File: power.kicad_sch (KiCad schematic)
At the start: 65 parts, among them Q10 2NPN, Q3 PMOS, Q4 PMOS, Q5 PMOS, Q6 PMOS, Q7 2NPN, Q9 2PNP, U21 TPS62410, U22 LDO-2V5

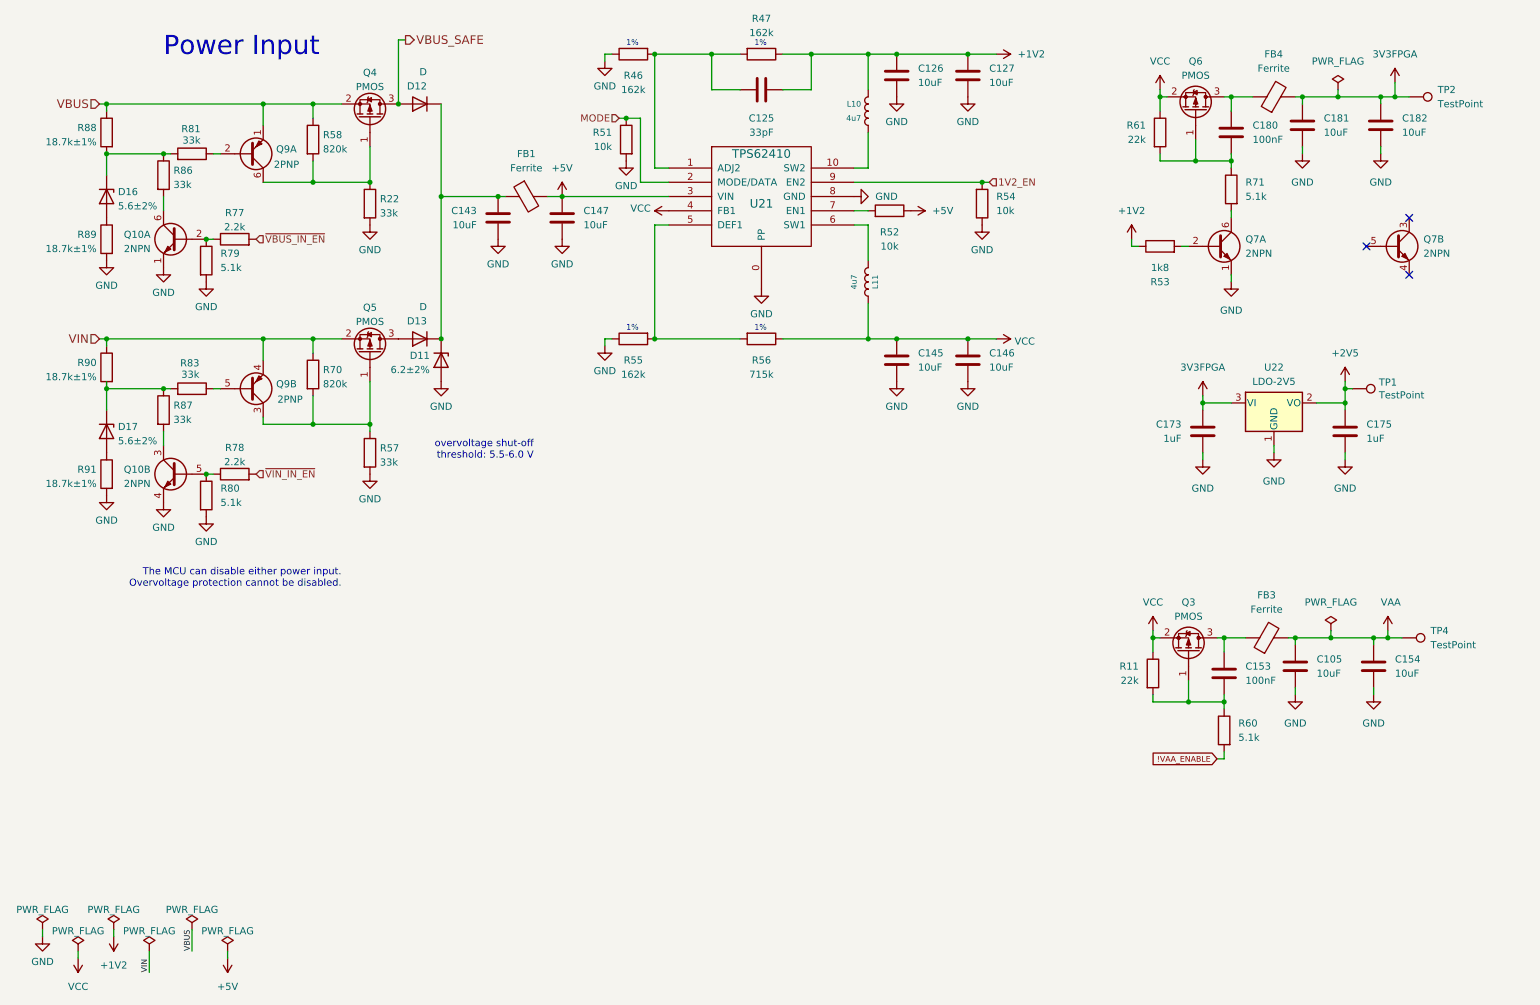
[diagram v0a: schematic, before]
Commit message: Rearrange RF section
- Use DPDT RF switches to reduce long tracks
- Add limiter
- Add switch control logic
- Move ADC/DAC U18 to RF area
- Remove baseband header P9
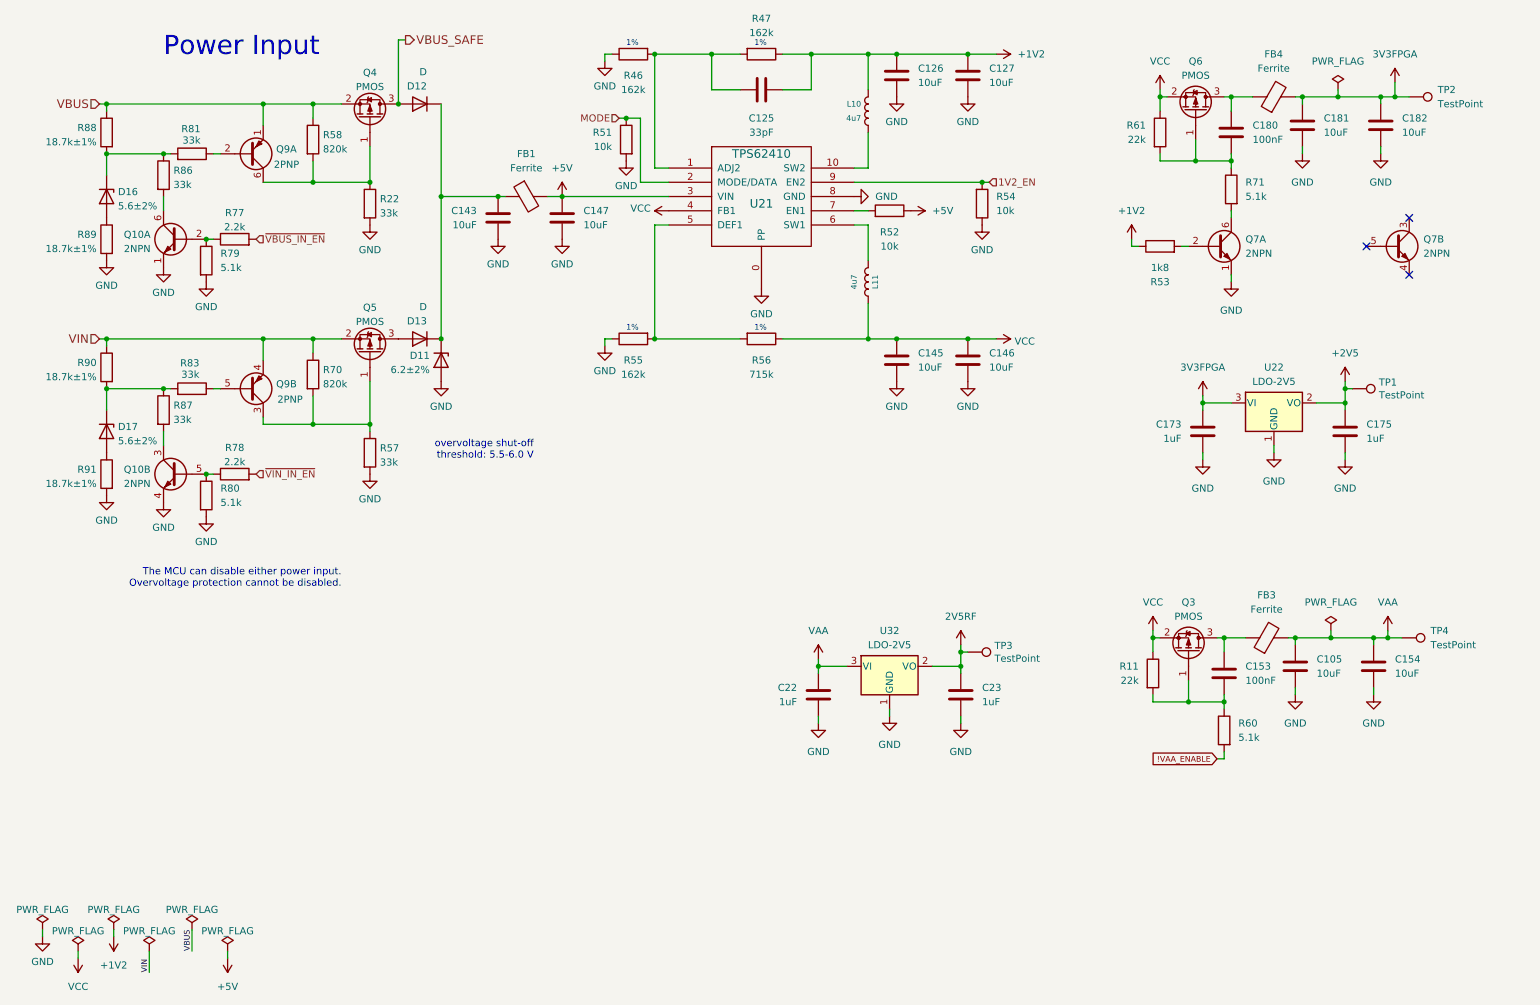
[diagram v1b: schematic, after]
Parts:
- added C22, C23: 1uF, Capacitor_SMD:C_0402_1005Metric, symbol Device:C
- added TP3: TestPoint, TestPoint:TestPoint_Pad_D1.0mm, symbol Connector:TestPoint
- added U32: LDO-2V5, Package_TO_SOT_SMD:SOT-23-3, symbol Regulator_Linear:XC6206PxxxMR
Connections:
- net GND: now also C22.2, C23.2, U32.1 (GND)
- net VAA: now also C22.1, U32.3 (VI)
- new net 2V5RF: C23.1, TP3.1, U32.2 (VO)

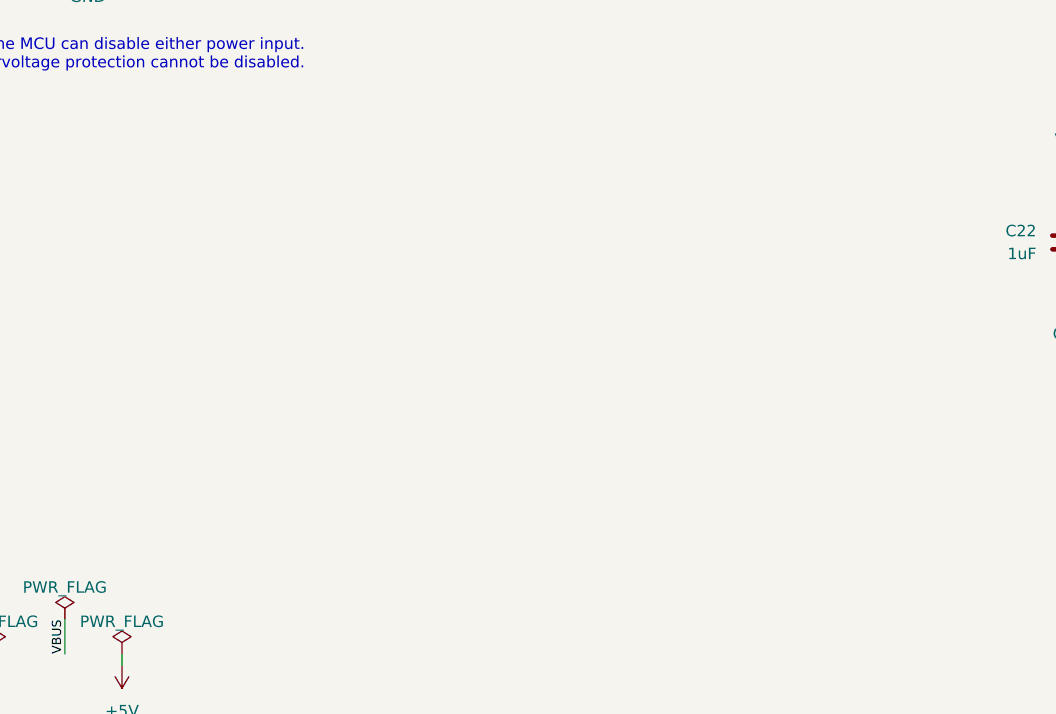
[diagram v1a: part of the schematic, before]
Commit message: Add current-limiting switch to expansion interface
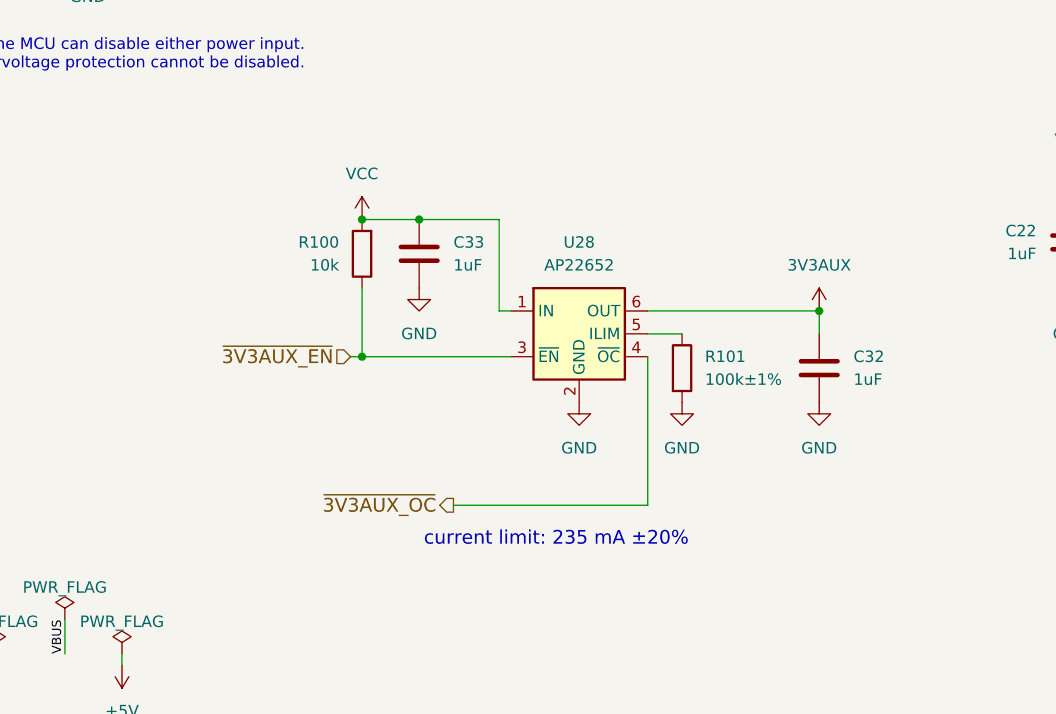
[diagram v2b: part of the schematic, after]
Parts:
- added C32, C33: 1uF, Capacitor_SMD:C_0402_1005Metric, symbol Device:C
- added R100: 10k, Resistor_SMD:R_0402_1005Metric, symbol Device:R
- added R101: 100k±1%, Resistor_SMD:R_0402_1005Metric, symbol Device:R
- added U28: AP22652, Package_SO:TSOP-6_1.65x3.05mm_P0.95mm, symbol Power_Management:BD2243G
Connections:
- net GND: now also C32.2, C33.2, R101.2, U28.2 (GND)
- net VCC: now also C33.1, R100.2, U28.1 (IN)
- new net: R101.1, U28.5 (ILIM)
- new net 3V3AUX: C32.1, U28.6 (OUT)
- new net ~{3V3AUX_EN}: R100.1, U28.3 (~{EN})
- new net ~{3V3AUX_OC}: U28.4 (~{OC})
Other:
- note added: "current limit: 235 mA ±20%"

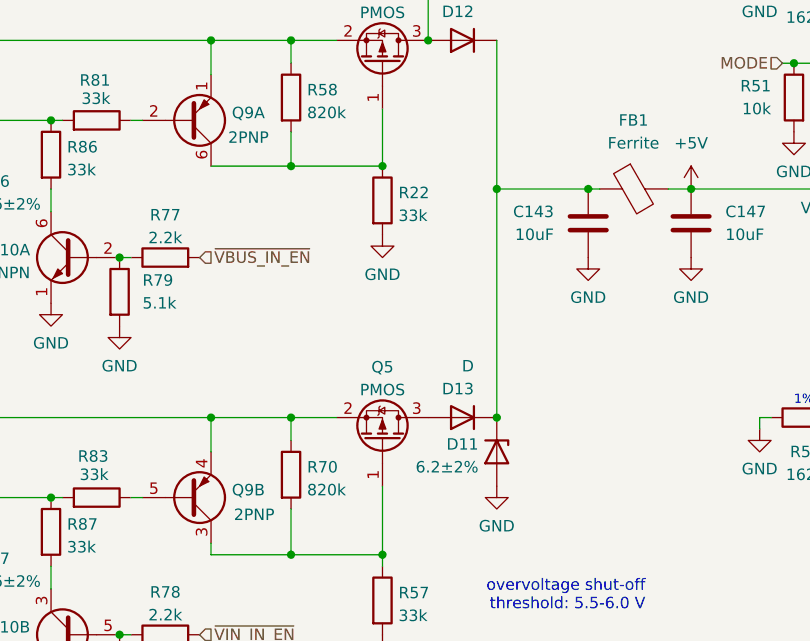
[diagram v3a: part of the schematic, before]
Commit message: Change Type-C controller U29 to HUSB328
- Update USB TVS
- Improve USB differential impedance
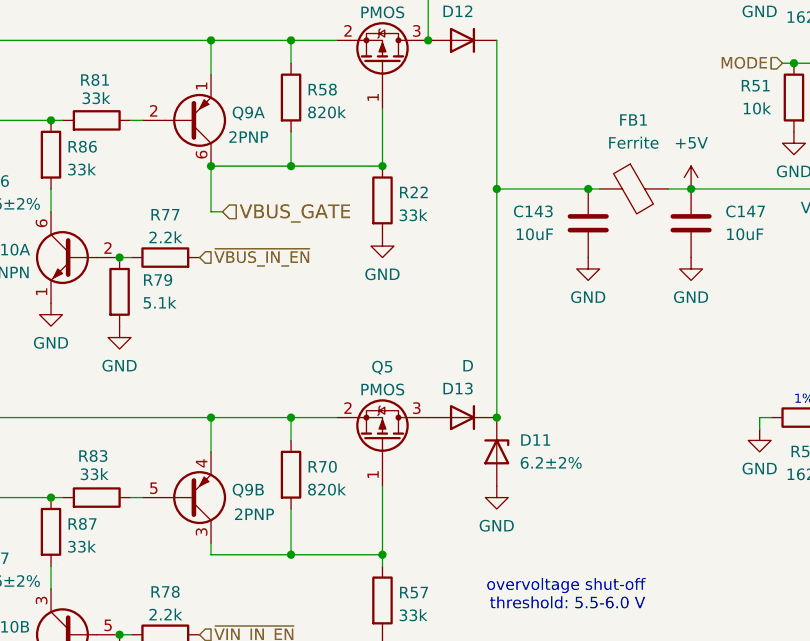
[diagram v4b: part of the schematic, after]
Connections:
- net VBUS_GATE: now reaches Q4.1 (G), Q9.6 (C1), R22.1, R58.2
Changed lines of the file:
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@@
 	)
 	(junction
+		(at 59.69 48.26)
+		(diameter 0)
+		(color 0 0 0 0)
+	)
+	(junction
 		(at 187.96 48.26)
 		(diameter 0)
@@
 	(wire
 		(pts
+			(xy 59.69 53.34) (xy 60.96 53.34)
+		)
+		(stroke
+			(width 0)
+			(type default)
+		)
+	)
+	(wire
+		(pts
 			(xy 129.54 45.72) (xy 129.54 25.4)
 		)
@@
 	(wire
 		(pts
+			(xy 59.69 48.26) (xy 59.69 53.34)
+		)
+		(stroke
+			(width 0)
+			(type default)
+		)
+	)
+	(wire
+		(pts
 			(xy 68.58 34.29) (xy 73.66 34.29)
 		)
@@
 		)
 	)
+	(hierarchical_label "VBUS_GATE"
+		(shape input)
+		(at 60.96 53.34 0)
+		(effects
+			(font
+				(size 1.524 1.524)
+			)
+			(justify left)
+		)
+	)
 	(hierarchical_label "MODE"
 		(shape input)
@@
 		(fields_autoplaced yes)
 		(property "Reference" "D11"
-			(at 89.408 79.1753 90)
+			(at 93.98 78.7399 90)
 			(effects
 				(font
 					(size 1.27 1.27)
 				)
-				(justify right)
+				(justify left)
 			)
 		)
 		(property "Value" "6.2±2%"
-			(at 89.408 81.7122 90)
+			(at 93.98 81.2799 90)
 			(effects
 				(font
 					(size 1.27 1.27)
 				)
-				(justify right)
+				(justify left)
 			)
 		)

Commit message: Consolidate PMOS component selection
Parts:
- Q3, Q6: Part Number YJL2301C -> YJL3401A
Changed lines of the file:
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@@
 			)
 		)
-		(property "Datasheet" "https://www.21yangjie.com/pdf/mosfet/YJL2301C.pdf"
+		(property "Datasheet" "https://www.21yangjie.com/pdf/mosfet/YJL3401A.pdf"
 			(at 224.79 132.08 0)
 			(effects
@@
 			)
 		)
-		(property "Part Number" "YJL2301C"
+		(property "Part Number" "YJL3401A"
 			(at 224.79 132.08 0)
 			(effects
@@
 			)
 		)
-		(property "Datasheet" "https://www.21yangjie.com/pdf/mosfet/YJL2301C.pdf"
+		(property "Datasheet" "https://www.21yangjie.com/pdf/mosfet/YJL3401A.pdf"
 			(at 226.06 35.56 0)
 			(effects
@@
 			)
 		)
-		(property "Part Number" "YJL2301C"
+		(property "Part Number" "YJL3401A"
 			(at 226.06 35.56 0)
 			(effects

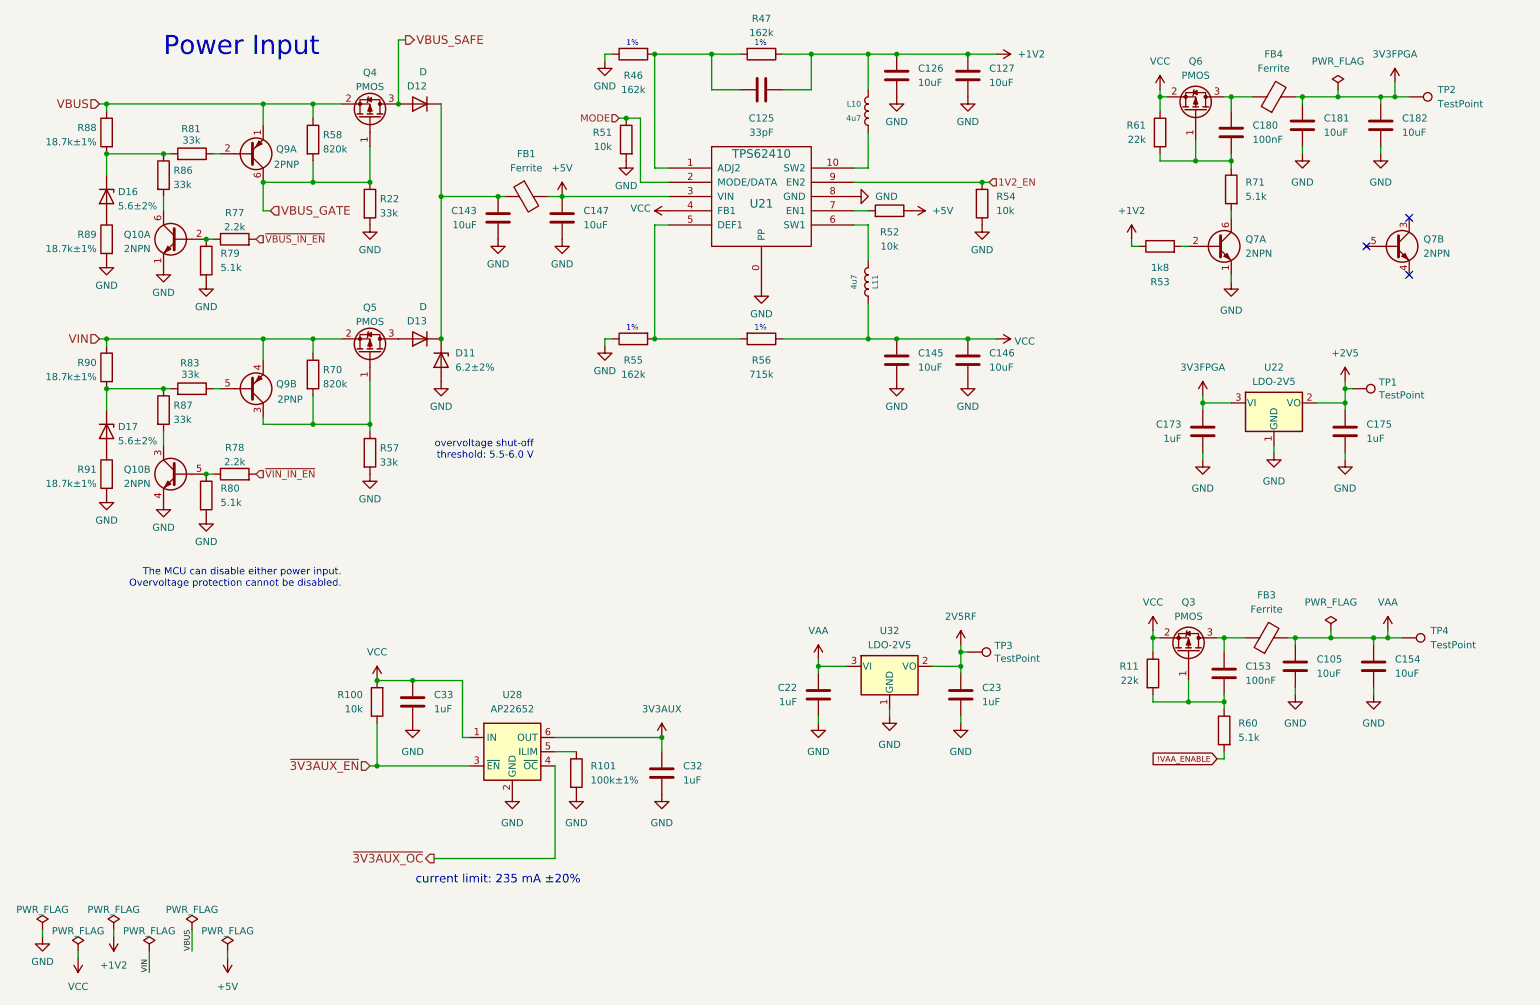
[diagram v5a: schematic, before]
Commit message: Improve power supply filtering and decoupling
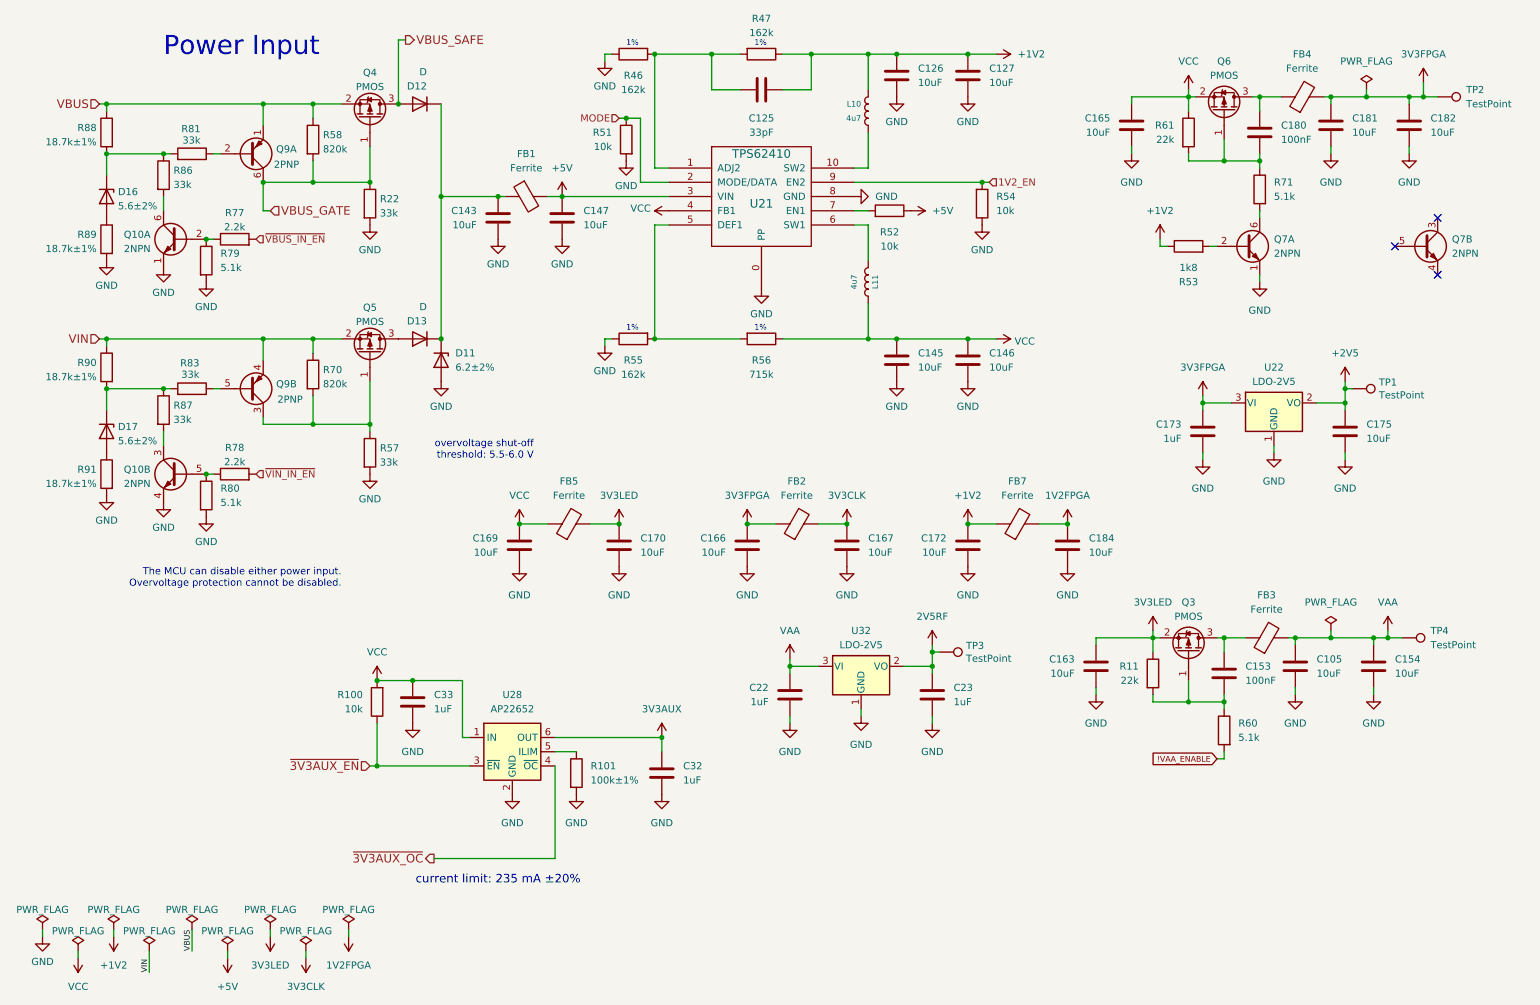
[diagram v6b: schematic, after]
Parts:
- added C163, C165, C166, C167, C169, C170, C172, C184: 10uF, Capacitor_SMD:C_0805_2012Metric, symbol Device:C
- added FB2, FB5, FB7: Ferrite, Inductor_SMD:L_0603_1608Metric, symbol Device:FerriteBead
- C175: value 1uF -> 10uF; footprint Capacitor_SMD:C_0402_1005Metric -> Capacitor_SMD:C_0805_2012Metric; Part Number CL05A105KA5NQNC -> CL21A106KOQNNNE; Substitution Murata GRM155R61E105KA12D -> Murata GRM21BR61A106KE19L
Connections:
- net +1V2: now also C172.1, FB7.1
- net 3V3FPGA: now also C166.1, FB2.1
- net GND: now also C163.2, C165.2, C166.2, C167.2, C169.2, C170.2, C172.2, C184.2
- net VCC: now also C165.1, C169.1, FB5.1; no longer Q3.2 (S), R11.1
- new net 1V2FPGA: C184.1, FB7.2
- new net 3V3CLK: C167.1, FB2.2
- new net 3V3LED: C163.1, C170.1, FB5.2, Q3.2 (S), R11.1
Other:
- moved on the sheet: C180, C181, C182, C22, C23, FB4, Q6, Q7A, Q7B, R53, R61, R71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

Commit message: Update component selections
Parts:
- R11, R61: Part Number RC0201JR-0722KL -> RC0201FR-0722K6L
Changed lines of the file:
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@@
 			)
 		)
-		(property "Description" "RES 22K OHM 5% 1/20W 0201"
+		(property "Description" "RES 22.6K OHM 1% 1/20W 0201"
 			(at 224.79 39.37 0)
 			(effects
@@
 			)
 		)
-		(property "Part Number" "RC0201JR-0722KL"
+		(property "Part Number" "RC0201FR-0722K6L"
 			(at 224.79 39.37 0)
 			(effects
@@
 			)
 		)
-		(property "Description" "RES 22K OHM 5% 1/20W 0201"
+		(property "Description" "RES 22.6K OHM 1% 1/20W 0201"
 			(at 218.44 135.89 0)
 			(effects
@@
 			)
 		)
-		(property "Part Number" "RC0201JR-0722KL"
+		(property "Part Number" "RC0201FR-0722K6L"
 			(at 218.44 135.89 0)
 			(effects
